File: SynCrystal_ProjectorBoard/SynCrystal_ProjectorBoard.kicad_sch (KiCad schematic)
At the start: 20 parts, among them J10 Screw_Terminal_01x03, J11 to DIN Traces, J5 Relais Board, J6 uC Cable, J7 to DIN Connector, J8 to Motor Ctrl PCB, J9 to Motor Controller Hat, SW6 SW_SPDT, U10 AP63205WU, U9 TS5A3357DCUR

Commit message: Projector PCB!
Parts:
- removed J11: to DIN Traces, symbol Connector:Conn_01x03_Pin
- removed J9: to Motor Controller Hat, symbol Connector:Conn_01x04_Socket
- removed SW6: SW_SPDT, symbol Switch:SW_SPDT
- removed U9: TS5A3357DCUR, easyeda2kicad:VSSOP-8_L2.4-W2.1-P0.50-LS3.2-BR, symbol easyEDA:TS5A3357DCUR_nicer
- added J3: to Lamp Relay Board, easyEDA:CONN-TH_5P-P2.50_ZX-XH2.54-5PZZ, symbol Connector_Generic:Conn_01x05
- added U2, U3, U4: TS5A3160DBVR-TP, easyEDA:SOT-23-6_L2.9-W1.6-P0.95-LS2.8-BR, symbol easyEDA:TS5A3160DBVR-TP_nicer
- J1: renamed from J8; footprint (none) -> easyEDA:CONN-TH_2P-P2.54_MX128-2.54-GN01-02P-CU-Y-A; LCSC (none) -> C5188442
- J2: renamed from J7; footprint (none) -> Peacemans Teile:PinHeader_1x03_P2.54mm_Vertical_BAUER; LCSC (none) -> C5188443
- J4: renamed from J10; value Screw_Terminal_01x03 -> to DIN Socket; footprint (none) -> easyEDA:CONN-TH_3P-P2.54_MX128-2.54-03P-GN01-CU-Y-A; LCSC (none) -> C5188443
- J5: footprint (none) -> easyEDA:HDR-TH_10P-P2.54-H-F-W10.0-N; LCSC (none) -> C2897392
- J6: footprint (none) -> Connector_PinHeader_2.54mm:PinHeader_1x10_P2.54mm_Horizontal
- JP1: renamed from JP3; footprint (none) -> Jumper:SolderJumper-2_P1.3mm_Open_TrianglePad1.0x1.5mm; now not fitted
- renumbered C17 to C1, C18 to C2, C19 to C3, C16 to C4, L2 to L1, R17 to R1, R12 to R2, R28 to R3, R27 to R4, U10 to U1
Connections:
- net +15V: now also J5.9 (Pin_9), J6.9 (Pin_9), J3.1 (Pin_1); no longer J5.2 (Pin_2), J6.2 (Pin_2)
- net +5V: now also J3.2 (Pin_2), U2.5 (V+), U3.5 (V+), U4.5 (V+)
- net Ctrl_V_in: now also J2.3 (Pin_3), U3.3
- net GND: now also J5.5 (Pin_5), J6.5 (Pin_5), J3.5 (Pin_5), U2.1, U2.2 (GND), U3.2 (GND), U4.2 (GND); no longer J5.6 (Pin_6), J6.6 (Pin_6)
- net M-Pin: now also J3.3 (Pin_3)
- net Pin_678: now also U4.4; no longer J2.3 (Pin_3), R3.2
- net at R1.1, R2.1, R4.2: now also U3.1
- net at J5.3 (Pin_3): now also J6.3 (Pin_3)
- net at J6.8 (Pin_8): now also U2.3; no longer J5.8 (Pin_8)
- net at R3.1: now also U3.4
- net DAC_en renamed DAC_EN
- net DAC_EN: now also U4.6 (IN)
- net Stop_en renamed Stop_EN
- net Stop_EN: now also J3.4 (Pin_4), U2.6 (IN), U3.6 (IN)
- new net: J5.8 (Pin_8), U2.4
- new net: J5.2 (Pin_2), J6.2 (Pin_2)
- new net: J5.6 (Pin_6), J6.6 (Pin_6)
- new net: R3.2, U4.1
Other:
- note added: "12-15V >"
- note added: "5V >"
- note added: "< (1) Stop_EN"
- note added: "< (4) Ctrl_V"
- note added: "< (5) ?"
- note added: "< (6) DAC_EN"
- note added: "> (2) M-Pin"
- note added: "> (3) 15V"
- note added: "GND"
- note added: "HELO <"
- note added: "M-Pin >"
- note removed: "<"
- note removed: ">"
- note removed: "Delete this copy!"
- note removed: "Pulses for the Monoflop"
- note removed: "Pulses for the Monoflop?"
- note removed: "consider a SPDT as input choice and a DPDT to disconnect 678 and the relais pulldown"
- note removed: "provide to ESS Follow-Start Hat: > Stop_en > Pulses for the Monoflop > Relais-Power > Monoflop Power To Do: - Monoflop for lamp control - 5V for the SP3T - consider a SPDT as input choice - and a DPDT to disconnect 678 and the relais pulldown"
- moved on the sheet: C1, C2, C3, C4, J1, J2, J4, J5, J6, L1, R1, R2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

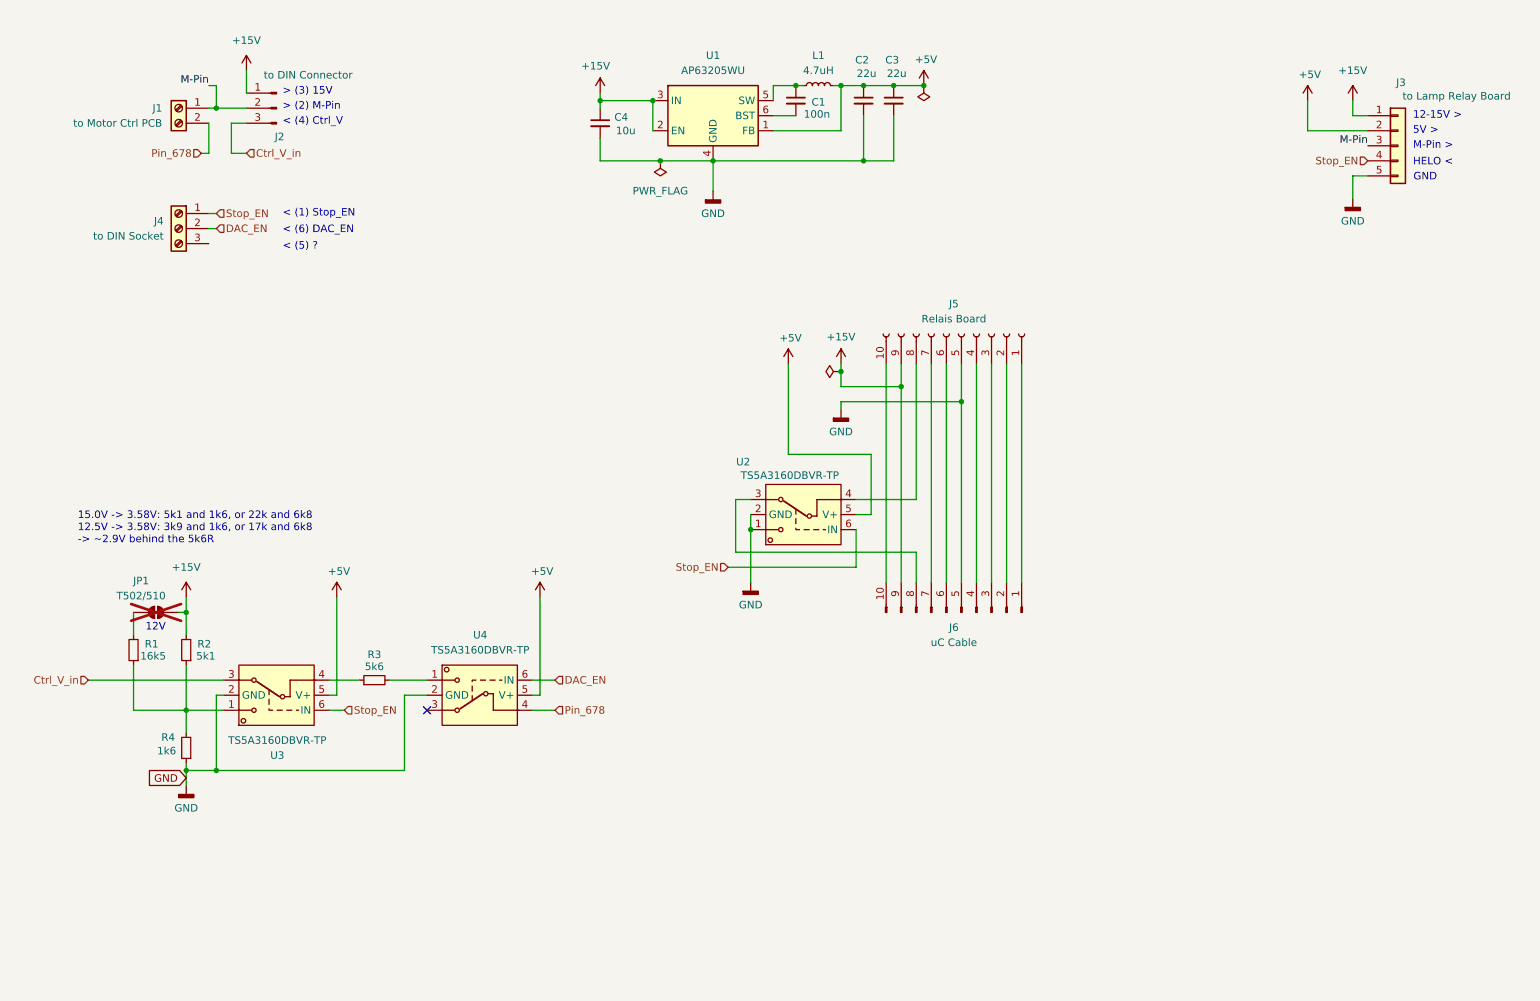
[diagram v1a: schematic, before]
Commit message: DRC for Projector Board happy
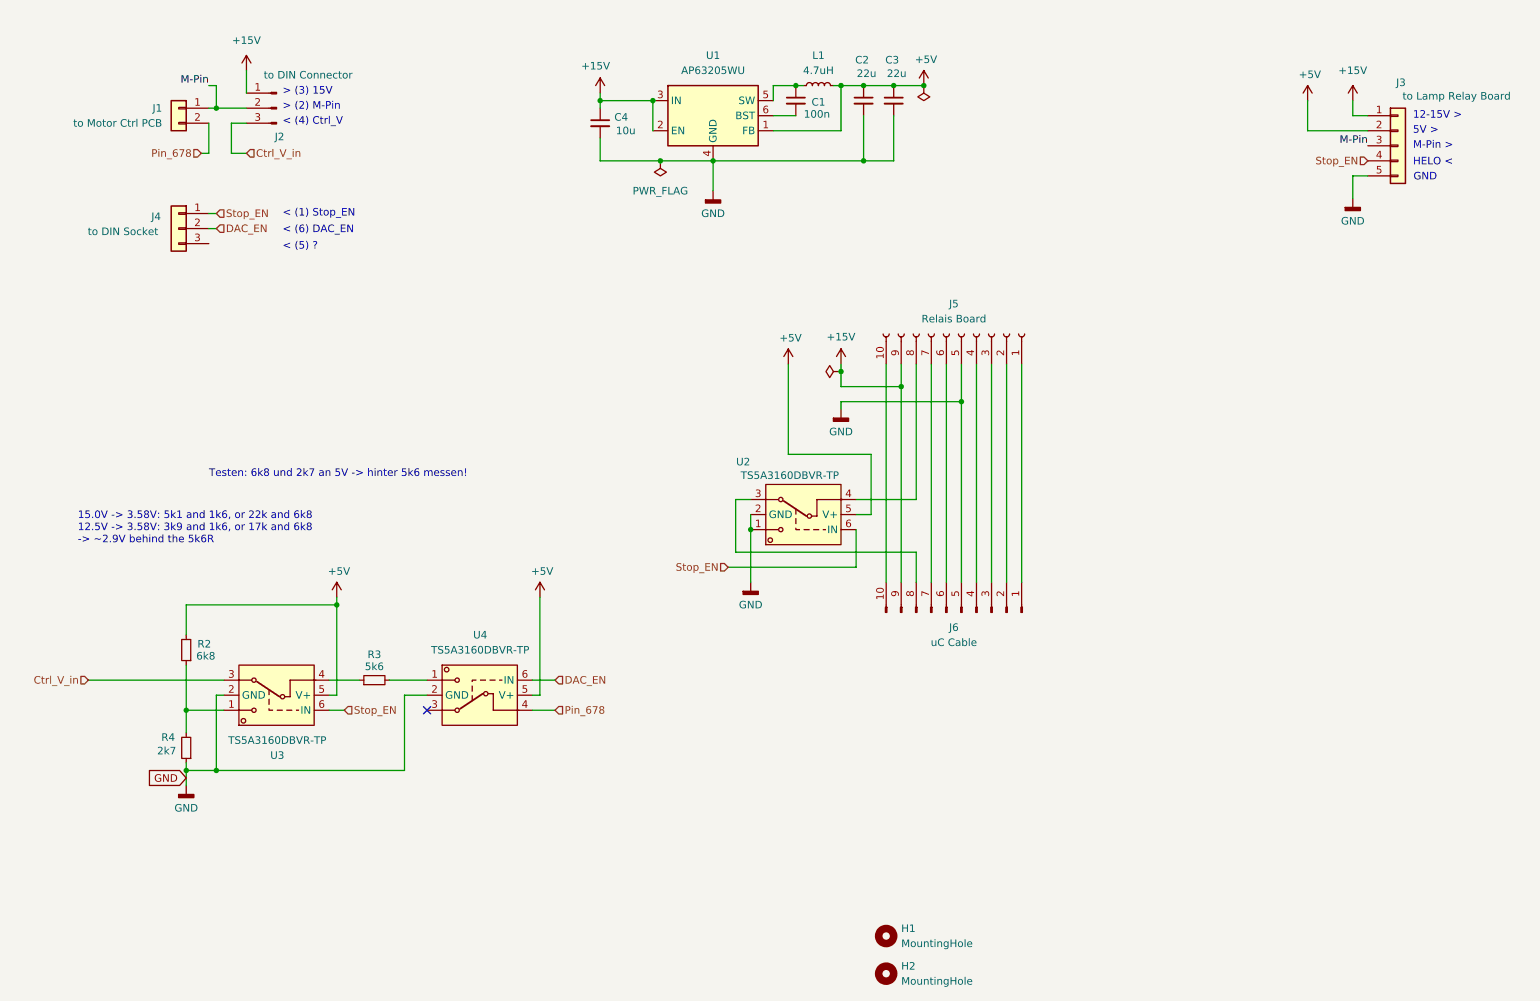
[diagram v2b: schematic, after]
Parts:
- removed JP1: T502/510, Jumper:SolderJumper-2_P1.3mm_Open_TrianglePad1.0x1.5mm, symbol Jumper:SolderJumper_2_Open
- removed R1: 16k5, Resistor_SMD:R_0603_1608Metric, symbol Device:R_Small
- added H1, H2: MountingHole, Peacemans Teile:MountingHole_2.1mm_just_hole, symbol Mechanical:MountingHole
- J1: footprint easyEDA:CONN-TH_2P-P2.54_MX128-2.54-GN01-02P-CU-Y-A -> easyEDA:CONN-TH_2P-P2.54_ZX-XH2.54-2PZZ-Y; symbol Connector:Screw_Terminal_01x02 -> Connector_Generic:Conn_01x02; LCSC C5188442 -> C22388684
- J4: footprint easyEDA:CONN-TH_3P-P2.54_MX128-2.54-03P-GN01-CU-Y-A -> easyEDA:CONN-TH_ZX-XH2.54-3PZZ-Y; symbol Connector:Screw_Terminal_01x03 -> Connector_Generic:Conn_01x03; LCSC C5188443 -> C22388685
- R2: value 5k1 -> 6k8
- R4: value 1k6 -> 2k7
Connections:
- net +15V: no longer R2.2
- net +5V: now also R2.2
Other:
- note added: "Testen: 6k8 und 2k7 an 5V -> hinter 5k6 messen!"
- note removed: "12V"

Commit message: More changes
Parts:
- removed H1, H2: MountingHole, Peacemans Teile:MountingHole_2.1mm_just_hole, symbol Mechanical:MountingHole
- removed U2: TS5A3160DBVR-TP, easyEDA:SOT-23-6_L2.9-W1.6-P0.95-LS2.8-BR, symbol easyEDA:TS5A3160DBVR-TP_nicer
- added Q1: AO3400A, Package_TO_SOT_SMD:SOT-23, symbol Transistor_FET:AO3400A
- added R1: 220, Resistor_SMD:R_0603_1608Metric, symbol Device:R_Small
- added R5, R6: 10k, Resistor_SMD:R_0603_1608Metric, symbol Device:R_Small
- J1: value to Motor Ctrl PCB -> to TCA955 PCB
- J2: value to DIN Connector -> to DIN connecting 3+1 Socket plug
- J4: value to DIN Socket -> to DIN Socket traces
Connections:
- net GND: now also J4.3 (Pin_3), Q1.2 (S), R5.1
- net Stop_EN: now also R1.1
- net at J6.8 (Pin_8): now also R6.1
- net at J5.8 (Pin_8): now also Q1.3 (D), R6.2
- new net: Q1.1 (G), R1.2, R5.2
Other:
- note added: "When the SynCrystal Controller is mounted internally, it connects to J2 and J4 instead of DIN-6."

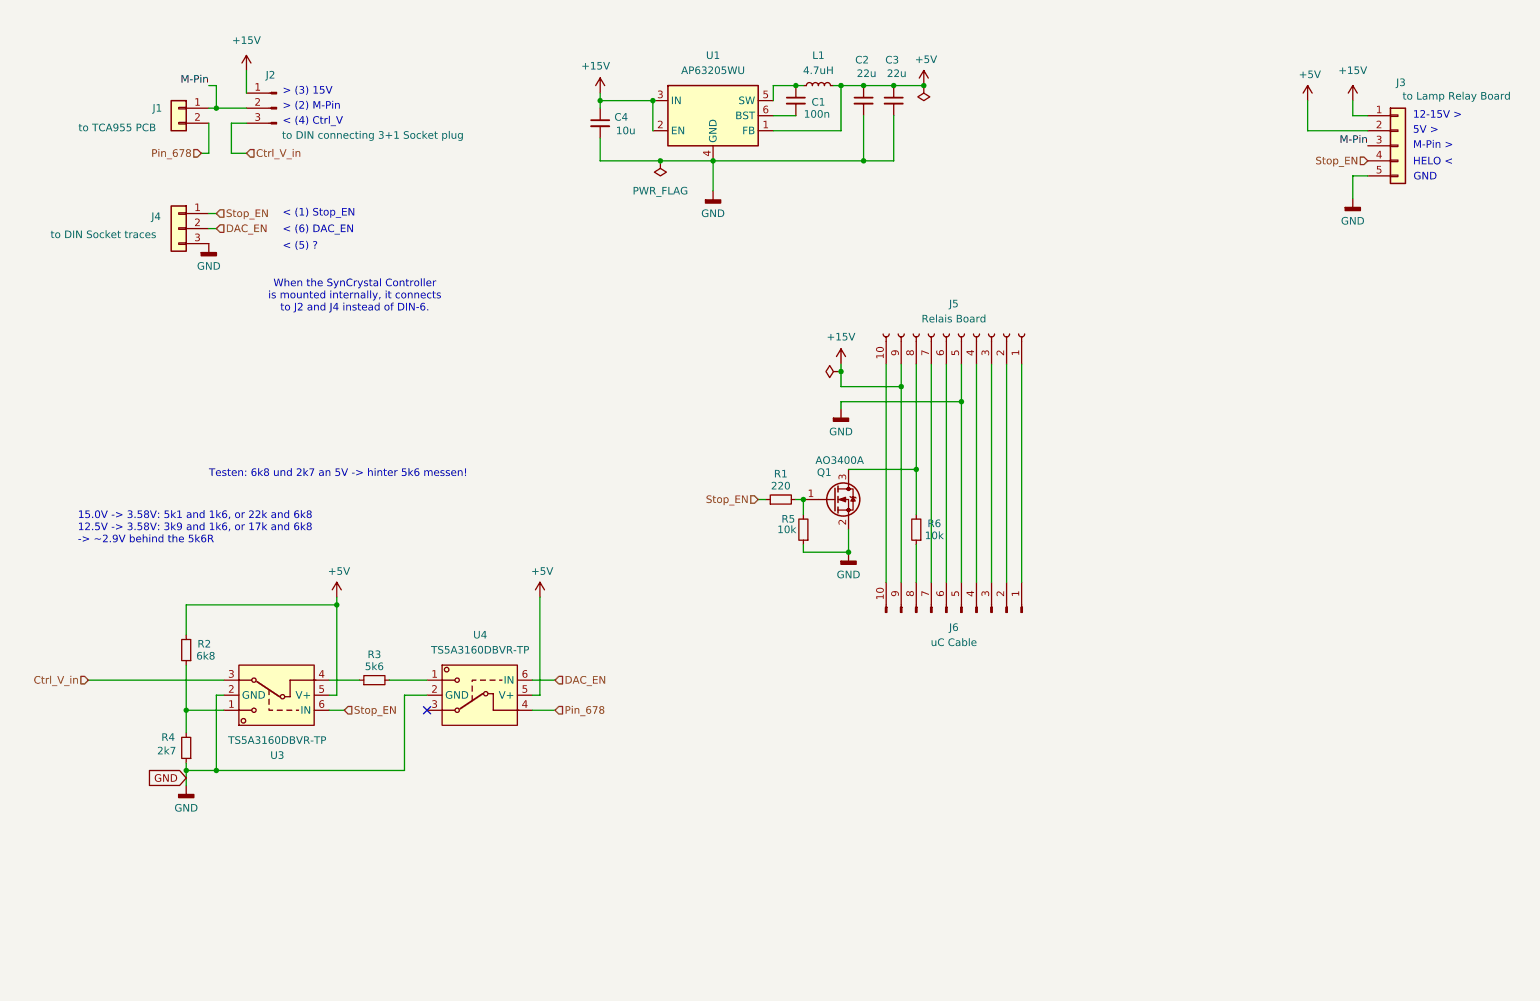
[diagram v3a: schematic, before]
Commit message: Starting to assign part numbers
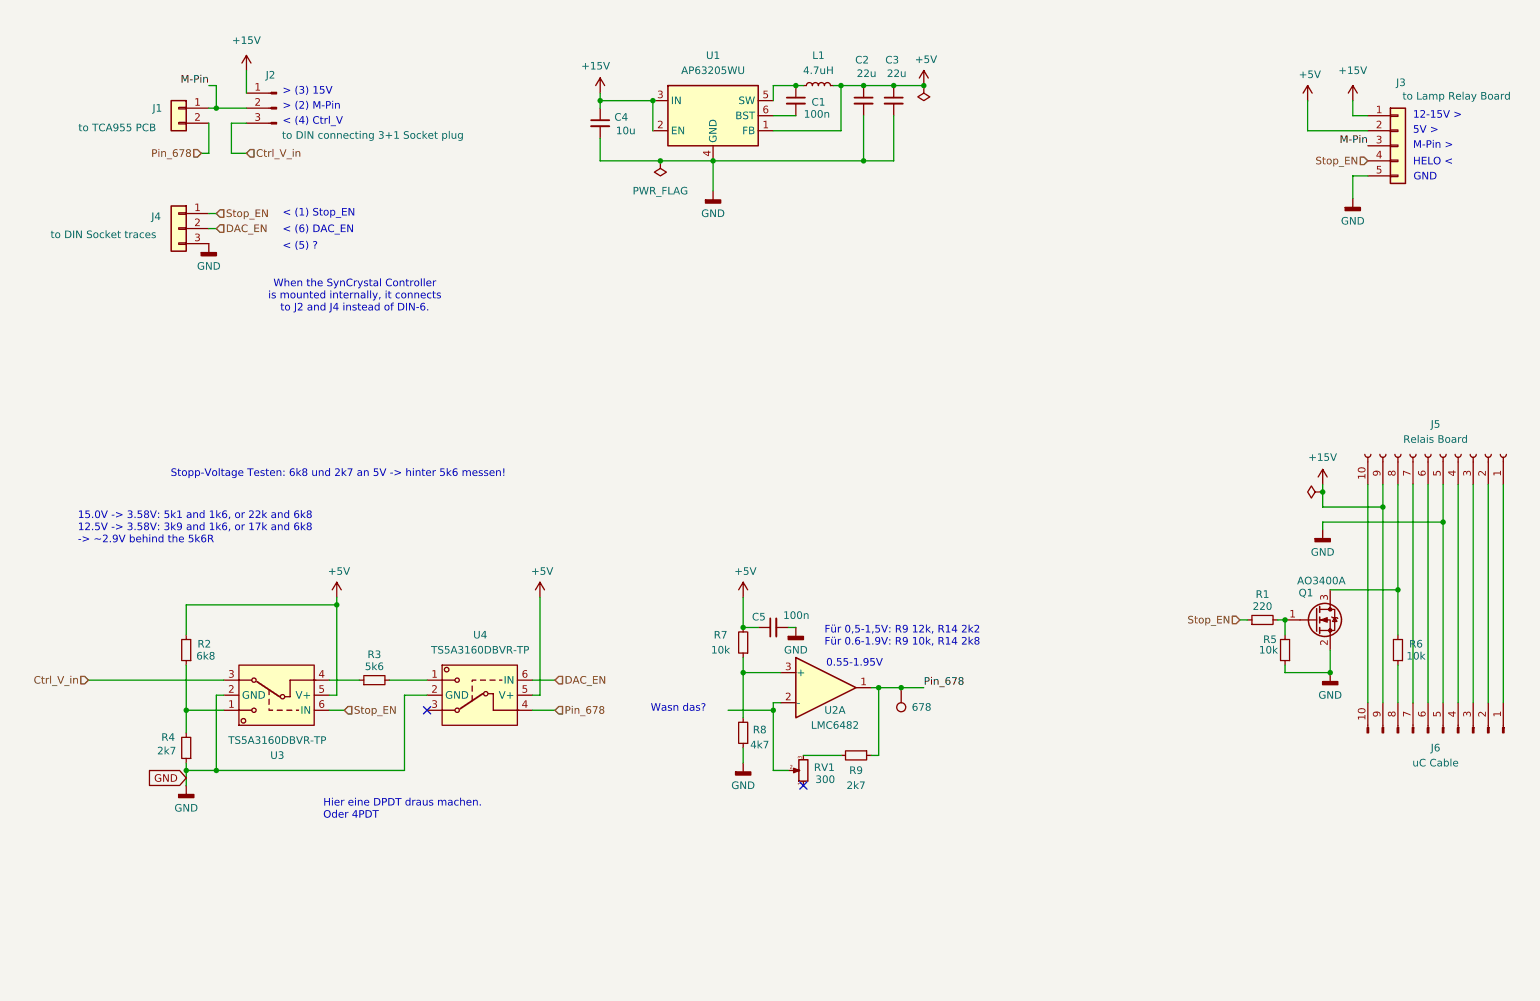
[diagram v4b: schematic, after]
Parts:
- added C5: 100n, Capacitor_SMD:C_0603_1608Metric, symbol Device:C_Small
- added R7: 10k, Resistor_SMD:R_0603_1608Metric, symbol Device:R_Small
- added R8: 4k7, Resistor_SMD:R_0603_1608Metric, symbol Device:R_Small
- added R9: 2k7, Resistor_SMD:R_0603_1608Metric, symbol Device:R_Small
- added RV1: 300, easyEDA:RES-SMD_RK10J11R0A0H, symbol Device:R_Potentiometer_Small
- added TP1: 678, TestPoint:TestPoint_Pad_D1.0mm, symbol Peacemans Teile:TestPoint_named
- added U2: LMC6482, Package_SO:SOIC-8_3.9x4.9mm_P1.27mm, symbol Amplifier_Operational:LMC6482
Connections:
- net +5V: now also C5.1, R7.2
- net GND: now also C5.2, R8.1
- net Pin_678: now also R9.1, TP1.1, U2.1
- new net: R9.2, RV1.3
- new net: R7.1, R8.2, U2.3 (+)
- new net: RV1.2, U2.2 (-)
- no-connect marks 1 -> 2
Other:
- note added: "0.55-1.95V"
- note added: "Für 0,5-1,5V: R9 12k, R14 2k2 Für 0.6-1.9V: R9 10k, R14 2k8"
- note added: "Hier eine DPDT draus machen. Oder 4PDT"
- note added: "Stopp-Voltage Testen: 6k8 und 2k7 an 5V -> hinter 5k6 messen!"
- note added: "Wasn das?"
- note removed: "Testen: 6k8 und 2k7 an 5V -> hinter 5k6 messen!"
- company: (none) -> filmkorn.org
- title: (none) -> SynCrystal Projector Board T610/T525
- moved on the sheet: J5, J6, Q1, R1, R5, R6
